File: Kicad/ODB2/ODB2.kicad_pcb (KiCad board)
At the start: 4 copper layers, 83.9 x 76.5 mm, 183 parts, among them J4 RF2-04A-T-00-50-G, J5 RFM_Conn_Coaxial, U1 STM32F412ZGTx, U10 W25Q512JVEIQ, U2 TLV2371DBV, U3 74LV1T87GVH, U5 L76L-M33, U6 ICM-20948, U7 MS580301BA01-00

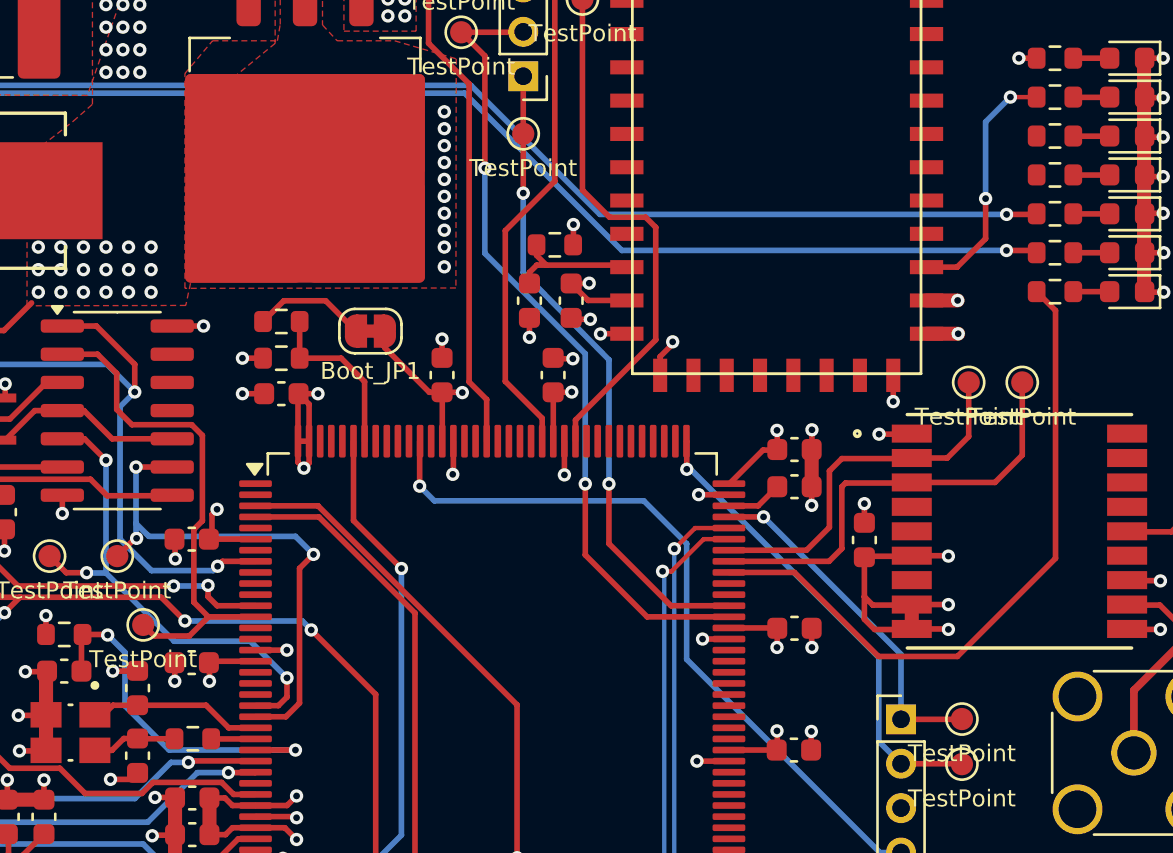
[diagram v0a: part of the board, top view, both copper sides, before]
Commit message: traces complétées
reste à nettoyer et optimiser le traçage
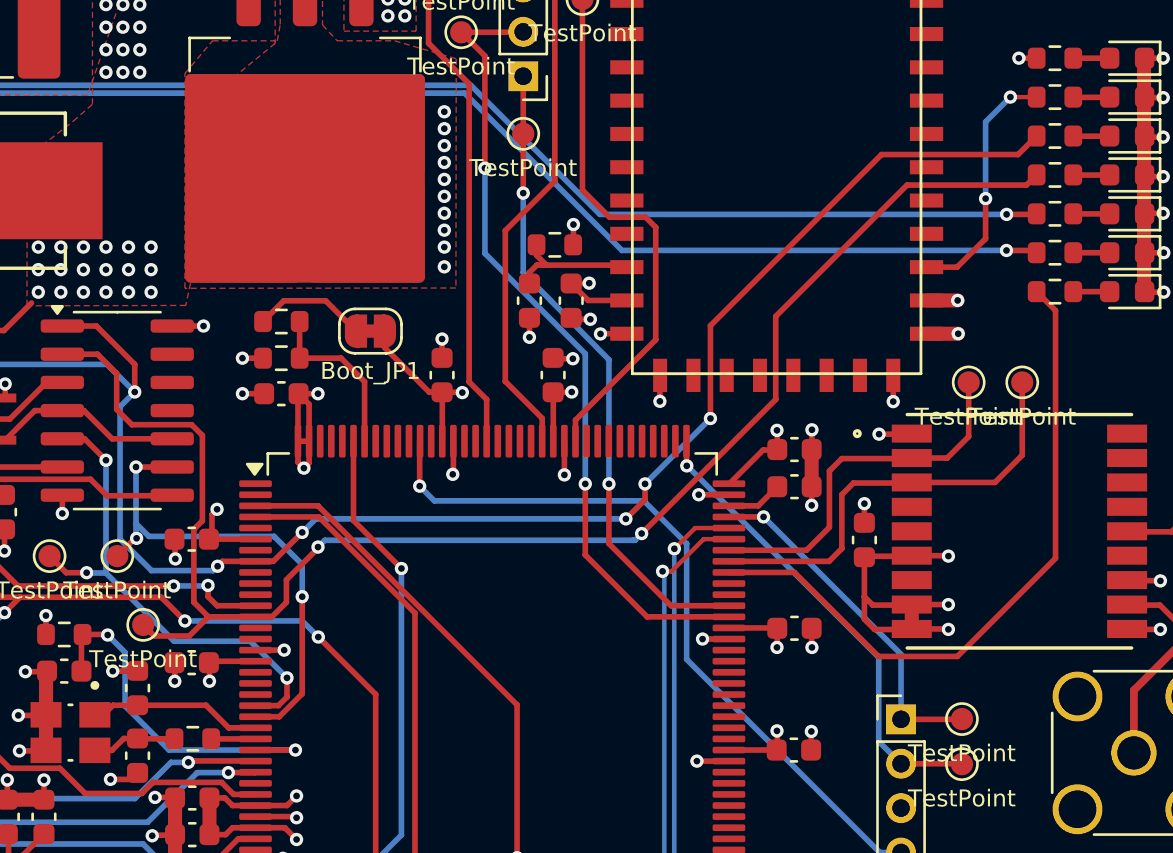
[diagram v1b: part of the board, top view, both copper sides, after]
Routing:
- net Pyros_Bluetooth: track 23.0 -> 69.3 mm, vias 0 -> 2
- net 7v4Enable: track 44.9 -> 90.9 mm, vias 3 -> 7
- net Pyros_DrogueODB: track 23.8 -> 22.7 mm
- net GND: track 156.3 -> 155.6 mm

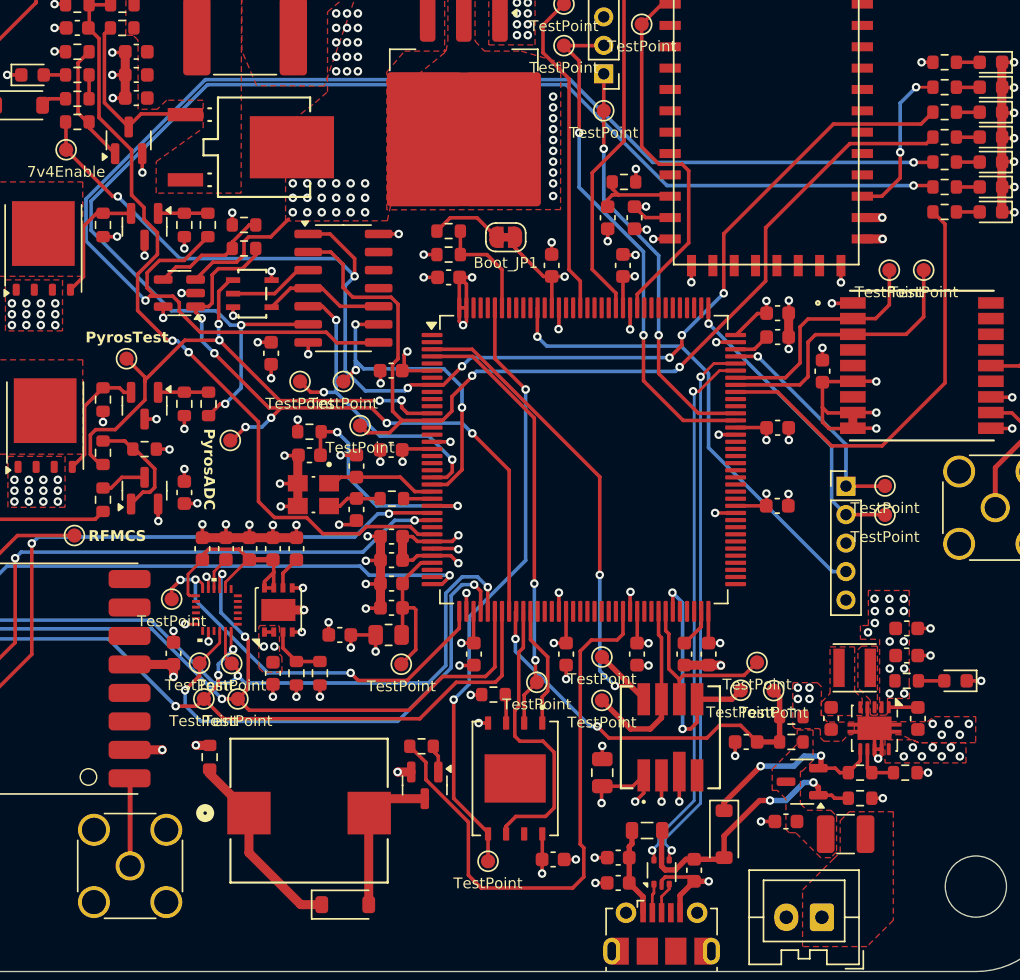
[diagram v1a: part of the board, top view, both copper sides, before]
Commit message: silkscreen pad tests
pas complet
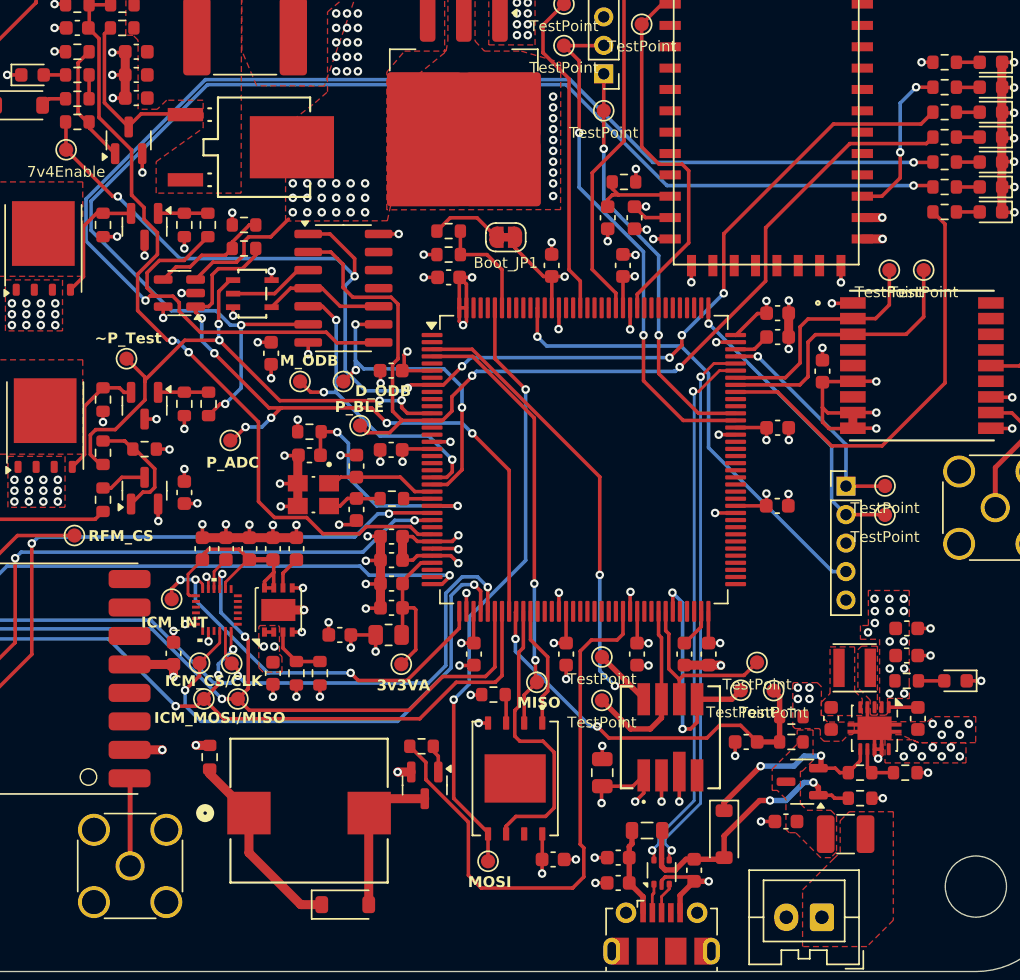
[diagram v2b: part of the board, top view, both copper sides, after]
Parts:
- TP2: value TestPoint -> INT
- TP3: value TestPoint -> CS
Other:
- board text added: "3v3VA"
- board text added: "D_ODB"
- board text added: "ICM_CS/CLK"
- board text added: "ICM_INT"
- board text added: "ICM_MOSI/MISO"
- board text added: "MISO"
- board text added: "MOSI"
- board text added: "M_ODB"
- board text added: "P_ADC"
- board text added: "P_BLE"
- board text added: "RFM_CS"
- board text added: "~P_Test"
- board text removed: "PyrosADC"
- board text removed: "PyrosTest"
- board text removed: "RFMCS"
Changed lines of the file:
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@@
 			(at 0 1.55 0)
 			(layer "F.SilkS")
+			(hide yes)
 			(effects
 				(font
@@
 			(at 0 1.55 0)
 			(layer "F.SilkS")
+			(hide yes)
 			(effects
 				(font
@@
 			(at 0 1.55 0)
 			(layer "F.SilkS")
+			(hide yes)
 			(effects
 				(font
@@
 			(at 0 1.55 0)
 			(layer "F.SilkS")
+			(hide yes)
 			(effects
 				(font
@@
 			(at 0 1.55 0)
 			(layer "F.SilkS")
+			(hide yes)
 			(effects
 				(font
@@
 			(at 0 1.55 0)
 			(layer "F.SilkS")
+			(hide yes)
 			(effects
 				(font
@@
 			(at 0 1.55 0)
 			(layer "F.SilkS")
+			(hide yes)
 			(effects
 				(font
@@
 			(at 0 1.55 0)
 			(layer "F.SilkS")
+			(hide yes)
 			(effects
 				(font
@@
 			(at 0 1.55 0)
 			(layer "F.SilkS")
+			(hide yes)
 			(effects
 				(font
@@
 			)
 		)
-		(property "Value" "TestPoint"
+		(property "Value" "CS"
 			(at 0 1.55 0)
 			(layer "F.SilkS")
+			(hide yes)
 			(effects
 				(font
@@
 			)
 		)
-		(property "Value" "TestPoint"
+		(property "Value" "INT"
 			(at 0 1.55 0)
 			(layer "F.SilkS")
+			(hide yes)
 			(effects
 				(font
@@
 		)
 	)
-	(gr_text "PyrosTest"
-		(at 15.4 32.35 0)
+	(gr_text "MOSI"
+		(at 42.2656 70.612 0)
 		(layer "F.SilkS")
 		(effects
@@
 		)
 	)
-	(gr_text "RFMCS"
+	(gr_text "~P_Test"
+		(at 16.0528 32.4104 0)
+		(layer "F.SilkS")
+		(effects
+			(font
+				(size 0.762 0.762)
+				(thickness 0.127)
+				(bold yes)
+			)
+			(justify left bottom)
+		)
+	)
+	(gr_text "M_ODB"
+		(at 29.0576 33.9852 0)
+		(layer "F.SilkS")
+		(effects
+			(font
+				(size 0.762 0.762)
+				(thickness 0.127)
+				(bold yes)
+			)
+			(justify left bottom)
+		)
+	)
+	(gr_text "RFM_CS"
 		(at 15.6 46.3 0)
 		(layer "F.SilkS")
@@
 		)
 	)
-	(gr_text "PyrosADC"
-		(at 23.65 38.3 -90)
+	(gr_text "D_ODB"
+		(at 34.3408 36.1188 0)
+		(layer "F.SilkS")
+		(effects
+			(font
+				(size 0.762 0.762)
+				(thickness 0.127)
+				(bold yes)
+			)
+			(justify left bottom)
+		)
+	)
+	(gr_text "P_ADC"
+		(at 23.876 41.148 0)
 		(layer "F.SilkS")
 		(effects
@@
 		)
 	)
+	(gr_text "ICM_MOSI/MISO"
+		(at 20.2184 59.0804 0)
+		(layer "F.SilkS")
+		(effects
+			(font
+				(size 0.762 0.762)
+				(thickness 0.127)
+				(bold yes)
+			)
+			(justify left bottom)
+		)
+	)
+	(gr_text "MISO"
+		(at 45.72 58.0136 0)
+		(layer "F.SilkS")
+		(effects
+			(font
+				(size 0.762 0.762)
+				(thickness 0.127)
+				(bold yes)
+			)
+			(justify left bottom)
+		)
+	)
+	(gr_text "P_BLE"
+		(at 32.9184 37.2364 0)
+		(layer "F.SilkS")
+		(effects
+			(font
+				(size 0.762 0.762)
+				(thickness 0.127)
+				(bold yes)
+			)
+			(justify left bottom)
+		)
+	)
+	(gr_text "3v3VA"
+		(at 35.8648 56.7944 0)
+		(layer "F.SilkS")
+		(effects
+			(font
+				(size 0.762 0.762)
+				(thickness 0.127)
+				(bold yes)
+			)
+			(justify left bottom)
+		)
+	)
 	(gr_text "7v4An"
 		(at 12.15 7.7 0)
@@
 		)
 	)
+	(gr_text "ICM_INT"
+		(at 19.304 52.3748 0)
+		(layer "F.SilkS")
+		(effects
+			(font
+				(size 0.762 0.762)
+				(thickness 0.127)
+				(bold yes)
+			)
+			(justify left bottom)
+		)
+	)
+	(gr_text "ICM_CS/CLK"
+		(at 20.9804 56.4896 0)
+		(layer "F.SilkS")
+		(effects
+			(font
+				(size 0.762 0.762)
+				(thickness 0.127)
+				(bold yes)
+			)
+			(justify left bottom)
+		)
+	)
 	(gr_text_box "78mm x 84mm"
 		(start -1.033 -3.9624)
@@
 		(start 73.7616 14.3256)
 		(end 74.9432 14.3256)
-		(width 0.2)
+		(width 0.254)
 		(layer "F.Cu")
 		(net 31)

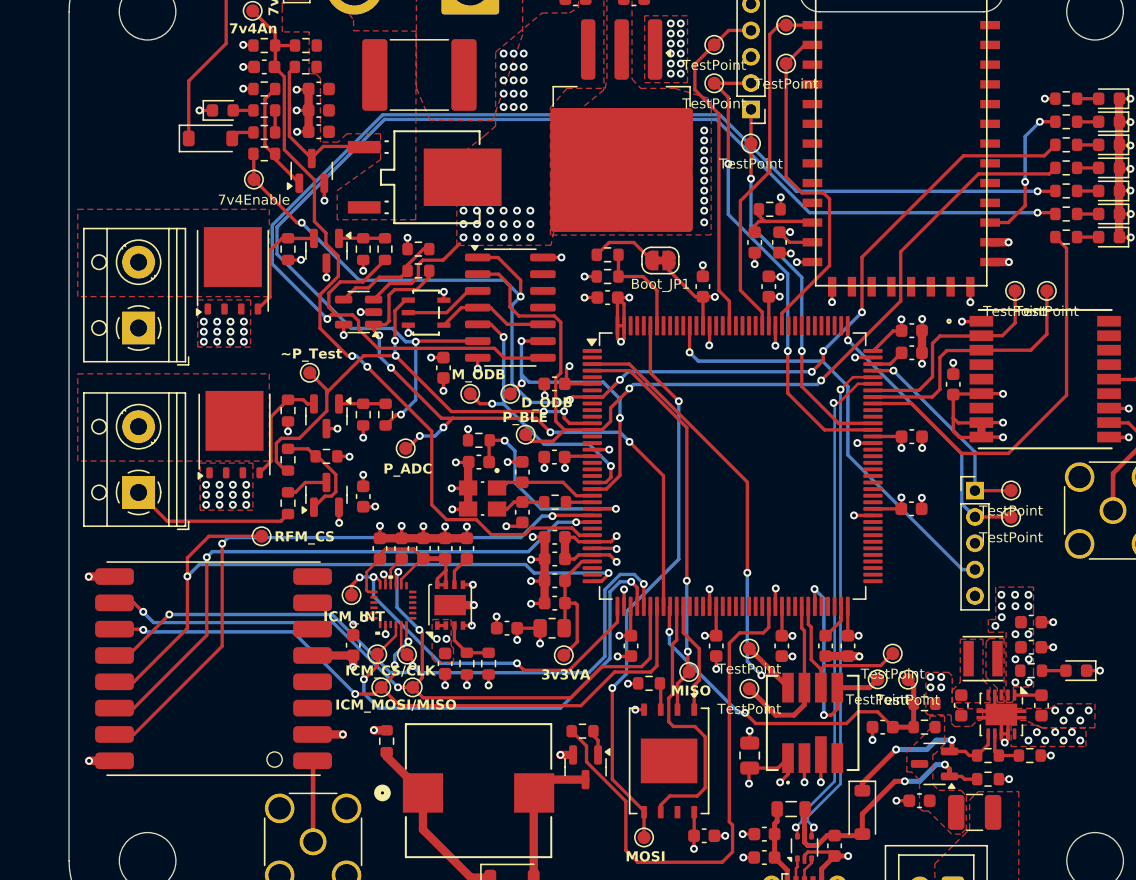
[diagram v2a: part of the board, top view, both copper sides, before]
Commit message: ajout .step + silkscreen
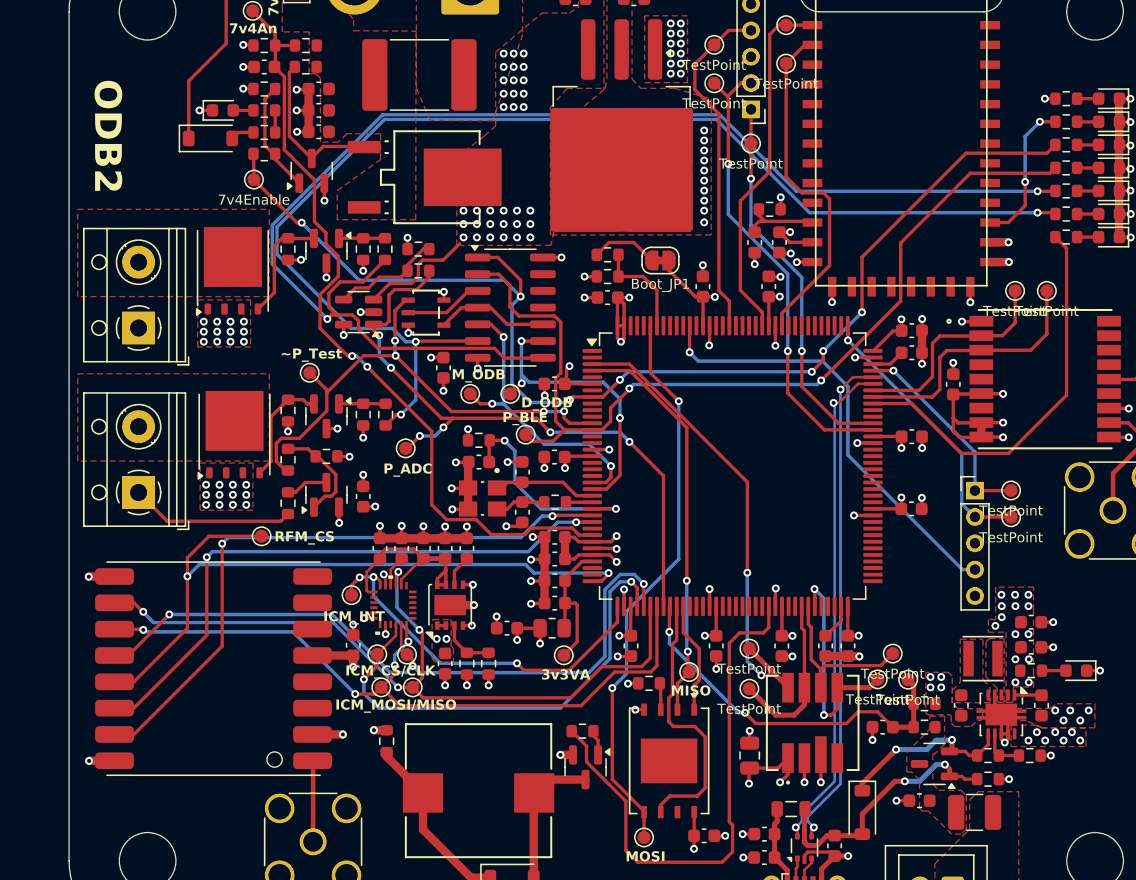
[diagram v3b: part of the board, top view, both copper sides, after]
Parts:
- added G***: LOGO, custom_footprints:GAUL_LOGO, F.Cu at (78.2, 25.4)
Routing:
- net UART6_RFD_TX: track 36.3 -> 35.7 mm
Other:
- board text added: "Lukas Dupuis Samuel Gagnon Mathis Tremblay Victor Deschênes Brieuc Soriano-Lohéac 02-2025 V1"
- board text added: "ODB2"
- board text removed: "Lukas Dupuis Samuel Gagnon Mathis Tremblay Victor Deschênes Brieuc Soriano-Lohéac"

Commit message: updated pcb
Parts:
- moved USB_Bus1 0.38 mm to (55.9, 73.4)
- moved Pyros_C1 0.15 mm to (28.4, 33.2)
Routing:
- net VCC: track 13.9 -> 21.3 mm, vias 2 -> 3
- net RFM_NIRQ: track 45.6 -> 50.5 mm
- net Pyros_MainOn: track 93.1 -> 90.2 mm
- net GND: track 155.6 -> 156.4 mm
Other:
- board text added: "3V7 IN"
- board text added: "7V4 IN"
- board text added: "BEACON"
- board text added: "GPS"
- board text added: "Luka Dupuis Samuel Gagnon Mathis Tremblay Victor Deschênes Brieuc Soriano-Lohéac 02-2025 V1"
- board text added: "RFD"
- board text added: "SPI4_BARO_CS"
- board text added: "SPI5_MISO"
- board text added: "SPI5_MOSI"
- board text added: "ST_LINK"
- board text removed: "Lukas Dupuis Samuel Gagnon Mathis Tremblay Victor Deschênes Brieuc Soriano-Lohéac 02-2025 V1"
- board text removed: "MISO"
- board text removed: "MOSI"
